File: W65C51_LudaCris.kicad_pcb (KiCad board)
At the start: 2 copper layers, 167.6 x 111.2 mm, 21 parts, among them J1 USB_RST, J2 USB_C, J3 BB816_BreakoutA27_PCIex16, J3 I2C, J5 USB_Status, J6 I2C, J7 I2C, U1 W65C51NxP, U10 74HC191, U11 ATF22V10, U12 ATF22V10, U13 74HC138, U14 74HC283, U17 MCP2221AxP, U18 MAX232, U19 74HC191, U4 74HC191, U5 74HC191, U6 1.8432 MHz, U8 74HC573, U9 74HC191

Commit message: GAL PLD
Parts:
- removed J1: USB_RST, Connector_PinHeader_2.54mm:PinHeader_1x02_P2.54mm_Horizontal
- removed J2: USB_C, Connector_USB:USB_C_Plug_JAE_DX07P024AJ1
- removed J3, J6: I2C, Connector_PinHeader_2.54mm:PinHeader_1x04_P2.54mm_Horizontal
- removed J3: BB816_BreakoutA27_PCIex16, BB816-MATX-PCIE:PCIexpress_x16_HW_FH
- removed J5: USB_Status, Connector_PinHeader_2.54mm:PinHeader_1x06_P2.54mm_Horizontal
- removed J7: I2C, Connector_PinHeader_2.54mm:PinHeader_1x03_P2.54mm_Horizontal
- removed U12: ATF22V10, Package_DIP:DIP-24_W7.62mm
- removed U13: 74HC138, Package_DIP:DIP-16_W7.62mm_Socket
- removed U14: 74HC283, Package_DIP:DIP-16_W7.62mm_Socket
- removed U17: MCP2221AxP, Package_DIP:DIP-14_W7.62mm
- removed U18: MAX232, Package_DIP:DIP-16_W7.62mm_Socket
- removed U19: 74HC191, Package_DIP:DIP-16_W7.62mm_Socket
- added C1: 100nF, Capacitor_THT:C_Disc_D3.4mm_W2.1mm_P2.50mm, F.Cu at (127.8, 132.8)
- added C10: 100nF, Capacitor_THT:C_Disc_D3.4mm_W2.1mm_P2.50mm, F.Cu at (119.3, 83.3)
- added C11: 100nF, Capacitor_THT:C_Disc_D3.4mm_W2.1mm_P2.50mm, F.Cu at (142.9, 83.3)
- added C12: 10uF, Capacitor_THT:CP_Radial_D4.0mm_P1.50mm, F.Cu at (134.8, 131.4)
- added C13: 1nF, Capacitor_THT:C_Disc_D3.4mm_W2.1mm_P2.50mm, F.Cu at (119.0, 89.9)
- added C2: 100nF, Capacitor_THT:C_Disc_D3.4mm_W2.1mm_P2.50mm, F.Cu at (137.7, 144.2)
- added C3: 100nF, Capacitor_THT:C_Disc_D3.4mm_W2.1mm_P2.50mm, F.Cu at (134.8, 128.1)
- added C4: 100nF, Capacitor_THT:C_Disc_D3.4mm_W2.1mm_P2.50mm, F.Cu at (113.4, 136.3)
- added C5: 100nF, Capacitor_THT:C_Disc_D3.4mm_W2.1mm_P2.50mm, F.Cu at (173.8, 129.0)
- added C6: 100nF, Capacitor_THT:C_Disc_D3.4mm_W2.1mm_P2.50mm, F.Cu at (94.8, 119.1)
- added C7: 100nF, Capacitor_THT:C_Disc_D3.4mm_W2.1mm_P2.50mm, F.Cu at (98.2, 96.8)
- added C8: 100nF, Capacitor_THT:C_Disc_D3.4mm_W2.1mm_P2.50mm, F.Cu at (141.5, 135.3)
- added C9: 100nF, Capacitor_THT:C_Disc_D3.4mm_W2.1mm_P2.50mm, F.Cu at (168.8, 96.6)
- added H1: MountingHole_Pad, MountingHole:MountingHole_3.2mm_M3_Pad, F.Cu at (209.2, 105.5)
- added H2: MountingHole_Pad, MountingHole:MountingHole_3.2mm_M3_Pad, F.Cu at (213.4, 145.0)
- added H3: MountingHole_Pad, MountingHole:MountingHole_3.2mm_M3_Pad, F.Cu at (212.9, 127.6)
- added R1: 50, Resistor_THT:R_Axial_DIN0207_L6.3mm_D2.5mm_P7.62mm_Horizontal, F.Cu at (118.8, 86.5)
- added U2: 74HC138, Package_DIP:DIP-16_W7.62mm_Socket, F.Cu at (134.7, 136.1)
- added U3: 74HC573, Package_DIP:DIP-20_W7.62mm_Socket, F.Cu at (142.4, 124.9)
- added U7: 74HC191, Package_DIP:DIP-16_W7.62mm_Socket, F.Cu at (87.3, 97.2)
- U10: value 74HC191 -> 74HC283
- U11: value ATF22V10 -> 74HC191; footprint Package_DIP:DIP-24_W7.62mm -> Package_DIP:DIP-16_W7.62mm_Socket
- U4, U5: value 74HC191 -> ATF22V10; footprint Package_DIP:DIP-16_W7.62mm_Socket -> Package_DIP:DIP-24_W7.62mm_Socket
- U6: value 1.8432 MHz -> 74HC191; footprint Oscillator:Oscillator_DIP-8 -> Package_DIP:DIP-16_W7.62mm_Socket
- U8: value 74HC573 -> 74HC191; footprint Package_DIP:DIP-20_W7.62mm_Socket -> Package_DIP:DIP-16_W7.62mm_Socket
- moved U5 88.2 mm to (173.7, 125.6), turned to 180 degrees
- moved U6 77.3 mm to (87.3, 123.5)
- moved U9 67.9 mm to (179.0, 100.4)
- moved U4 66.9 mm to (107.3, 132.3), turned to 180 degrees
- moved U8 55.4 mm to (144.6, 143.3), turned to 90 degrees
- moved U11 30.3 mm to (145.9, 90.9), turned to 90 degrees
- moved U10 26.7 mm to (122.2, 91.1), turned to 90 degrees
- moved U1 17.7 mm to (112.5, 96.5)
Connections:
- net /~{IRQ1} renamed /~{IRQ}
- U1 pad 10: TxD -> /TxD
- U1 pad 11: unconnected-(U1-~{DTR}-Pad11) -> /~{DTR}
- U1 pad 12: RxD -> /RxD
- U1 pad 13: /A0 -> /RS0
- U1 pad 14: /A1 -> /RS1
- U1 pad 16: GND -> /~{DCD}
- U1 pad 2: VCC -> /CS1
- U1 pad 28: /~{WR} -> /R~{W}
- U1 pad 3: /~{IOCS1} -> /~{CS2}
- U1 pad 5: unconnected-(U1-RxC-Pad5) -> /RxC
- U1 pad 7: unconnected-(U1-XTAL2-Pad7) -> /XTAL2
- U1 pad 8: unconnected-(U1-~{RTS}-Pad8) -> /~{RTS}
- U1 pad 9: GND -> /~{CTS}
- U10 pad 1: /Q9 -> Net-(U10-S2)
- U10 pad 10: /Q10 -> Net-(U10-S4)
- U10 pad 11: /~{BAUD_LOAD} -> GND
- U10 pad 12: unconnected-(U10-MAX/MIN-Pad12) -> GND
- U10 pad 13: Net-(U10-~{RCO}) -> Net-(U10-S3)
- U10 pad 14: Net-(U10-CLK) -> GND
- U10 pad 15: /Q8 -> VCC
- U10 pad 2: unconnected-(U10-Qb-Pad2) -> VCC
- U10 pad 3: unconnected-(U10-Qa-Pad3) -> /CR6
- U10 pad 4: /~{CTEN} -> Net-(U10-S1)
- U10 pad 5: VCC -> /CR5
- U10 pad 6: unconnected-(U10-Qc-Pad6) -> GND
- U10 pad 7: unconnected-(U10-Qd-Pad7) -> /CR7
- U10 pad 9: /Q11 -> unconnected-(U10-C4-Pad9)
- U11 pad 1: VCC -> Net-(U10-S2)
- U11 pad 10: GND -> Net-(U10-S3)
- U11 pad 11: GND -> /~{TX_START}
- U11 pad 12: GND -> unconnected-(U11-MAX/MIN-Pad12)
- U11 pad 13: GND -> /~{TX_COMPLETE}
- U11 pad 14: /~{CTEN} -> /~{BAUD_CLK}
- U11 pad 15: /CTL_REG_WR -> Net-(U10-S1)
- U11 pad 16: /Q8 -> VCC
- U11 pad 2: /CR0 -> unconnected-(U11-Qb-Pad2)
- U11 pad 3: /CR1 -> unconnected-(U11-Qa-Pad3)
- U11 pad 4: /CR2 -> /~{CTEN}
- U11 pad 5: /CR3 -> VCC
- U11 pad 9: GND -> Net-(U10-S4)
- U4 pad 1: Net-(U14-S2) -> VCC
- U4 pad 10: Net-(U14-S3) -> GND
- U4 pad 11: /~{TX_START} -> GND
- U4 pad 12: unconnected-(U4-MAX/MIN-Pad12) -> GND
- U4 pad 13: /~{TX_COMPLETE} -> /~{BAUD_CLK}
- U4 pad 14: /~{BAUD_CLK} -> /~{DSR}
- U4 pad 15: Net-(U14-S1) -> /~{BAUD_LOAD}
- U4 pad 16: VCC -> /~{CTEN}
- U4 pad 2: unconnected-(U4-Qb-Pad2) -> /CR0
- U4 pad 3: unconnected-(U4-Qa-Pad3) -> /CR1
- U4 pad 4: /~{CTEN} -> /CR2
- U4 pad 5: VCC -> /CR3
- U4 pad 6: unconnected-(U4-Qc-Pad6) -> /~{CTL_REG_WR}
- U4 pad 7: unconnected-(U4-Qd-Pad7) -> /~{TX_START}
- U4 pad 8: GND -> /~{TX_COMPLETE}
- U4 pad 9: Net-(U14-S4) -> GND
- U5 pad 1: /Q5 -> VCC
- U5 pad 10: /Q6 -> GND
- U5 pad 11: /~{BAUD_LOAD} -> GND
- U5 pad 12: unconnected-(U5-MAX/MIN-Pad12) -> GND
- U5 pad 13: Net-(U10-CLK) -> GND
- U5 pad 14: Net-(U19-~{RCO}) -> unconnected-(U5-I/O-Pad14)
- U5 pad 15: /Q4 -> unconnected-(U5-I/O-Pad15)
- U5 pad 16: unconnected-(U5-VCC-Pad16) -> /Q8
- U5 pad 2: unconnected-(U5-Qb-Pad2) -> /CR0
- U5 pad 3: unconnected-(U5-Qa-Pad3) -> /CR1
- U5 pad 4: /~{CTEN} -> /CR2
- U5 pad 5: VCC -> /CR3
- U5 pad 6: unconnected-(U5-Qc-Pad6) -> GND
- U5 pad 7: unconnected-(U5-Qd-Pad7) -> GND
- U5 pad 9: /Q7 -> GND
- U6 pad 1: VCC -> GND
- U6 pad 4: GND -> /~{CTEN}
- U6 pad 5: /XTAL1 -> VCC
- U6 pad 8: VCC -> GND
- U8 pad 1: GND -> /Q9
- U8 pad 10: GND -> /Q10
- U8 pad 11: /CTL_REG_WR -> /~{BAUD_LOAD}
- U8 pad 12: /CR7 -> unconnected-(U8-MAX/MIN-Pad12)
- U8 pad 13: /CR6 -> Net-(U8-~{RCO})
- U8 pad 14: /CR5 -> Net-(U7-~{RCO})
- U8 pad 15: /CR4 -> /Q8
- U8 pad 16: /CR3 -> VCC
- U8 pad 2: /D0 -> unconnected-(U8-Qb-Pad2)
- U8 pad 3: /D1 -> unconnected-(U8-Qa-Pad3)
- U8 pad 4: /D2 -> /~{CTEN}
- U8 pad 5: /D3 -> VCC
- U8 pad 6: /D4 -> unconnected-(U8-Qc-Pad6)
- U8 pad 7: /D5 -> unconnected-(U8-Qd-Pad7)
- U8 pad 8: /D6 -> GND
- U8 pad 9: /D7 -> /Q11
- U9 pad 14: Net-(U10-~{RCO}) -> Net-(U8-~{RCO})
- U9 pad 16: unconnected-(U9-VCC-Pad16) -> VCC
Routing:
- added copper zone on In1.Cu, net GND
- added copper zone on In2.Cu, net GND
- added copper zone on B.Cu, net VCC
- added copper zone on F.Cu, net VCC
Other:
- board size 167.6 x 111.2 mm -> 125.1 x 102.4 mm
- copper layers 2 -> 4

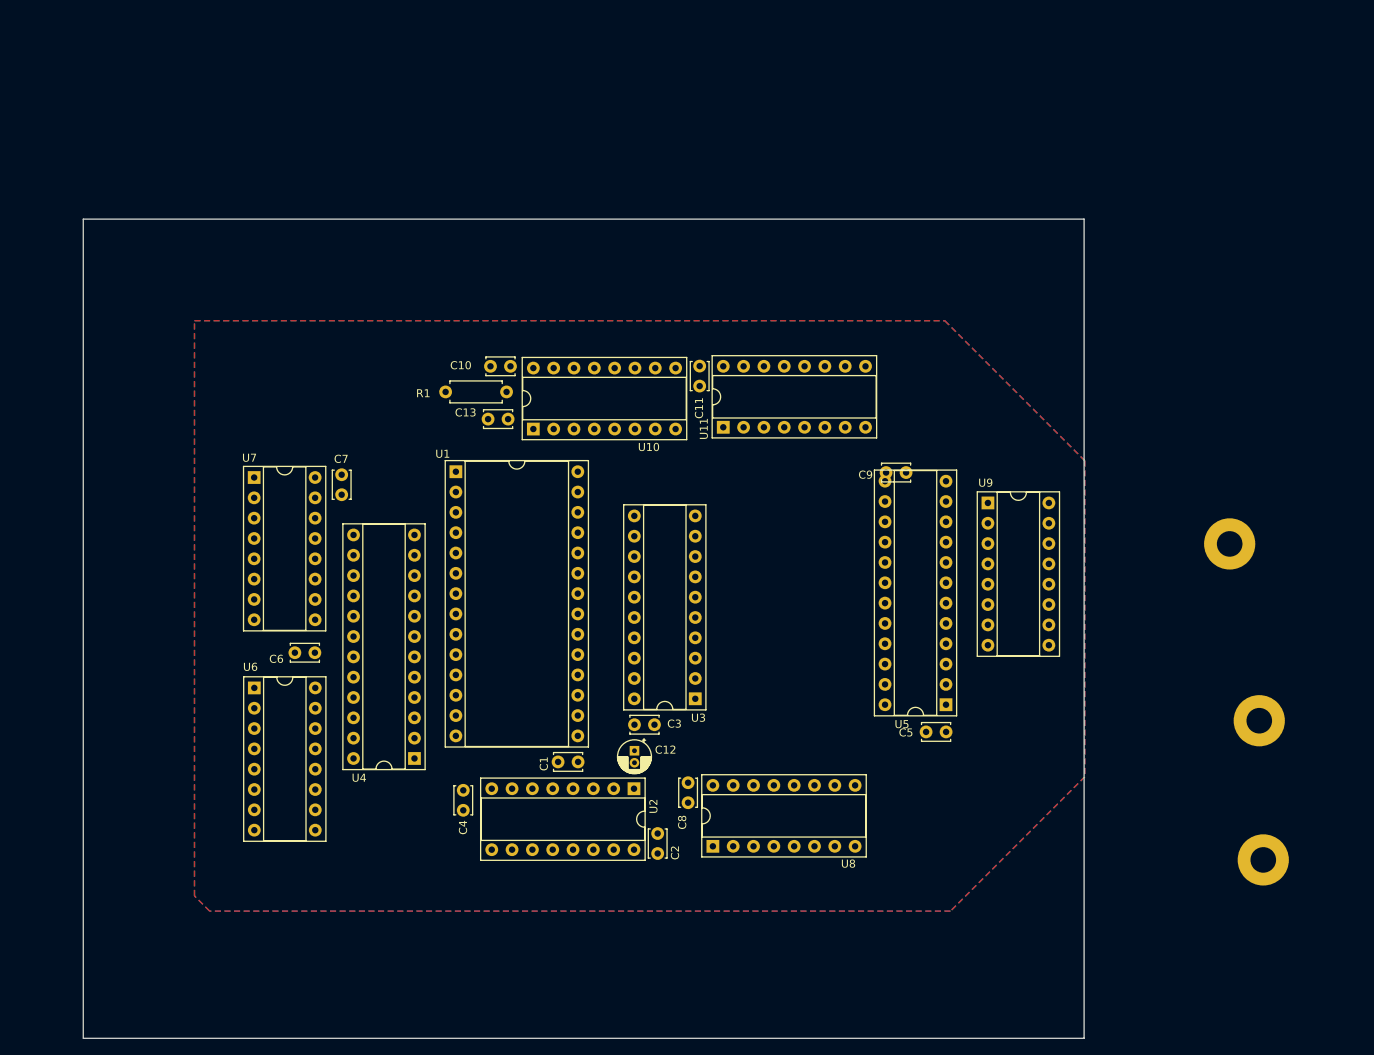
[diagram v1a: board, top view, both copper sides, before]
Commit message: PCB 2.54mm centres
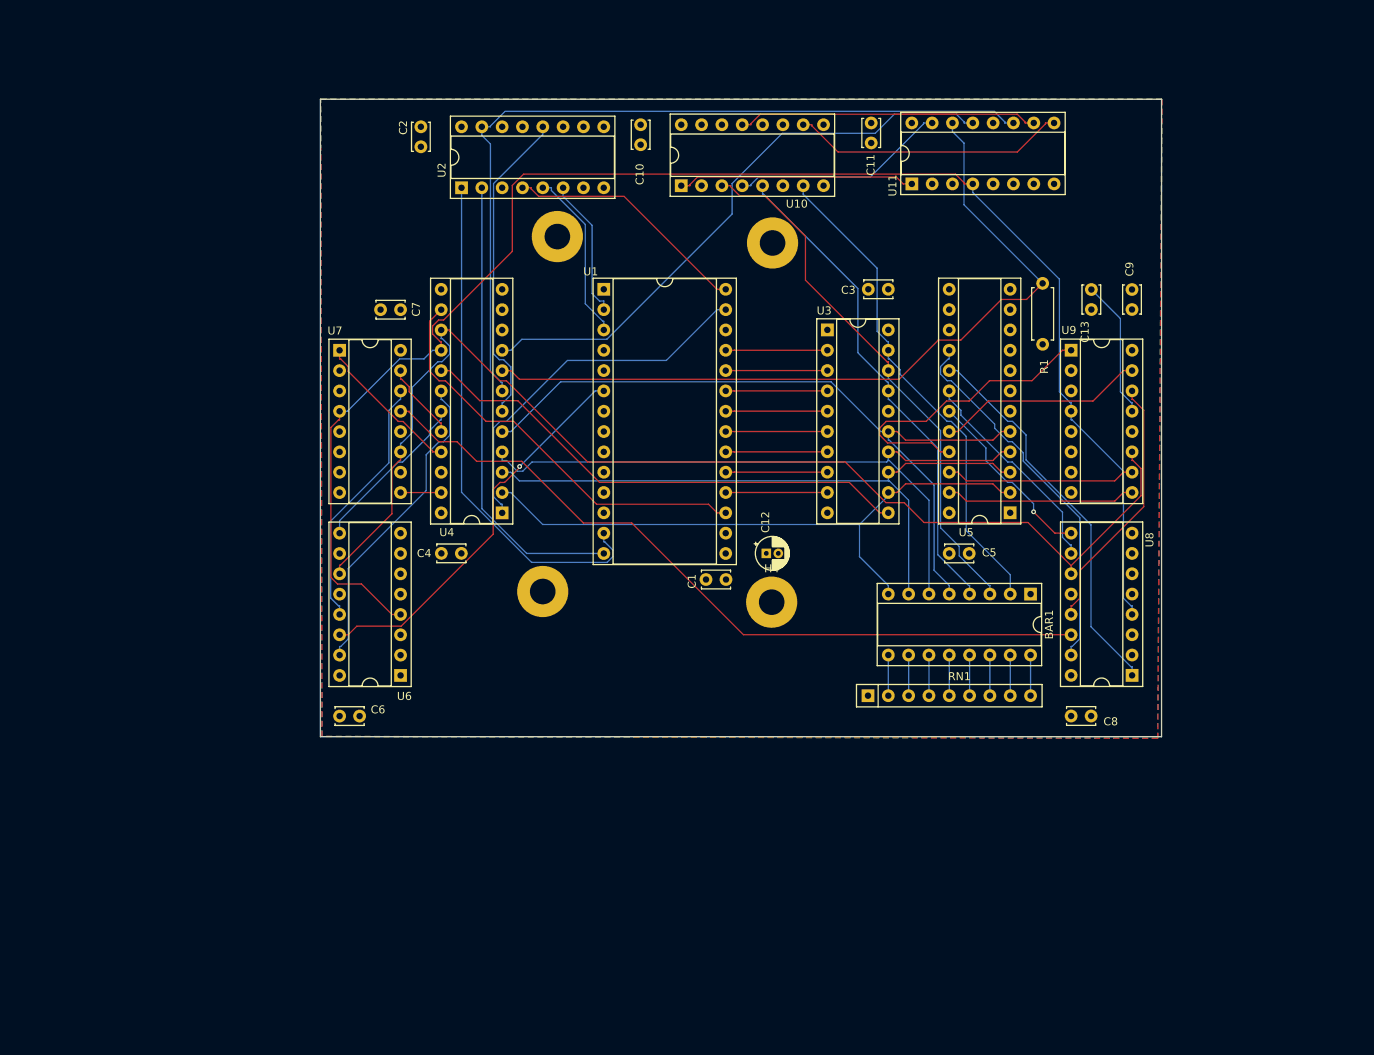
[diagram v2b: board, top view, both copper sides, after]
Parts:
- added BAR1: LED-Array-8, Package_DIP:DIP-16_W7.62mm_Socket, F.Cu at (184.3, 111.8)
- added H4: MountingHole_Pad, MountingHole:MountingHole_3.2mm_M3_Pad, F.Cu at (151.9, 112.8)
- added RN1: 220, Resistor_THT:R_Array_SIP9, F.Cu at (164.0, 124.5)
- moved H3 106.6 mm to (125.2, 67.1)
- moved H2 96.1 mm to (123.3, 111.5)
- moved C2 95.5 mm to (108.1, 53.4), turned to -90 degrees
- moved U2 78.2 mm to (113.2, 61.0), turned to 90 degrees
- moved C13 74.7 mm to (191.9, 73.7), turned to -90 degrees
- moved H1 68.4 mm to (152.1, 67.9)
- moved R1 68.4 mm to (185.8, 72.9), turned to -90 degrees
- moved C3 63.0 mm to (166.5, 73.7), turned to 180 degrees
- moved U8 56.6 mm to (197.0, 121.9), turned to 180 degrees
- moved U3 49.0 mm to (158.9, 78.8), turned to 0 degrees
- moved C8 48.6 mm to (189.4, 127.0), turned to 0 degrees
- moved U11 38.5 mm to (169.5, 60.5)
- moved C11 37.2 mm to (164.4, 52.9)
- moved U10 35.6 mm to (140.7, 60.7)
- moved C9 34.8 mm to (197.0, 76.2), turned to 90 degrees
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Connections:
- net /CTL_REG_WR renamed /CTL_REG_LOAD
- U3 pad 12: /CR7 -> /CR0
- U3 pad 13: /CR6 -> /CR1
- U3 pad 14: /CR5 -> /CR2
- U3 pad 15: /CR4 -> /CR3
- U3 pad 16: /CR3 -> /CR4
- U3 pad 17: /CR2 -> /CR5
- U3 pad 18: /CR1 -> /CR6
- U3 pad 19: /CR0 -> /CR7
- U3 pad 2: /D0 -> /D7
- U3 pad 3: /D1 -> /D6
- U3 pad 4: /D2 -> /D5
- U3 pad 5: /D3 -> /D4
- U3 pad 6: /D4 -> /D3
- U3 pad 7: /D5 -> /D2
- U3 pad 8: /D6 -> /D1
- U3 pad 9: /D7 -> /D0
- U4 pad 1: VCC -> /CLK
- U4 pad 13: /~{BAUD_CLK} -> GND
- U4 pad 8: /~{TX_COMPLETE} -> /~{BAUD_CLK}
- U4 pad 9: GND -> /~{TX_COMPLETE}
- U5 pad 1: VCC -> GND
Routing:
- net /~{CTEN}: track 0.00 -> 194.5 mm
- net /~{BAUD_LOAD}: track 0.00 -> 147.6 mm
- net /~{BAUD_CLK}: track 0.00 -> 121.5 mm
- net /~{TX_START}: track 0.00 -> 102.1 mm
- net Net-(U7-~{RCO}): track 0.00 -> 95.5 mm
- net /CR3: track 0.00 -> 93.2 mm
- net /CR2: track 0.00 -> 86.5 mm
- net /CR1: track 0.00 -> 81.2 mm
- net /CR0: track 0.00 -> 78.1 mm
- net /~{TX_COMPLETE}: track 0.00 -> 73.8 mm
- net /CR6: track 0.00 -> 67.6 mm
- net /RS0: track 0.00 -> 64.4 mm
- net /CTL_REG_LOAD: track 0.00 -> 63.3 mm
- net /CR7: track 0.00 -> 62.2 mm
- net /CR5: track 0.00 -> 62.1 mm
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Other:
- board size 125.1 x 102.4 mm -> 105.1 x 79.7 mm

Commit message: pcb
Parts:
- removed BAR1: LED-Array-8, Package_DIP:DIP-16_W7.62mm_Socket
- removed RN1: 220, Resistor_THT:R_Array_SIP9
- added J1: Conn_01x14, Connector_PinHeader_2.54mm:PinHeader_1x14_P2.54mm_Vertical, B.Cu at (133.5, 73.7)
- added J2: Conn_01x14, Connector_PinHeader_2.54mm:PinHeader_1x14_P2.54mm_Vertical, B.Cu at (148.8, 73.7)
- moved C2 60.8 mm to (119.1, 113.1), turned to 90 degrees
- moved U2 57.8 mm to (122.1, 118.1)
- moved U8 41.4 mm to (155.9, 117.2), turned to 90 degrees
- moved C8 39.6 mm to (155.9, 105.8)
- moved C10 38.3 mm to (170.0, 69.8), turned to 90 degrees
- moved U11 34.6 mm to (134.9, 62.3), turned to -90 degrees
- moved C11 30.8 mm to (138.7, 69.9), turned to 90 degrees
- moved H4 27.6 mm to (179.5, 113.5)
- moved H1 26.1 mm to (178.1, 65.8)
- moved U10 26.0 mm to (166.6, 62.2), turned to -90 degrees
- moved H2 22.8 mm to (145.8, 115.6)
- moved C13 17.6 mm to (176.3, 81.9), turned to 180 degrees
- moved C9 16.3 mm to (181.7, 81.9), turned to 180 degrees
- moved U9 16.1 mm to (174.1, 86.4)
- moved H3 15.9 mm to (109.6, 63.7)
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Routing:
- net /~{TX_COMPLETE}: track 73.8 -> 12.3 mm
- net /~{TX_START}: track 102.1 -> 44.1 mm
- net /CR3: track 93.2 -> 45.0 mm
- net /~{CTEN}: track 194.5 -> 148.3 mm
- net /CR6: track 67.6 -> 22.7 mm
- net /RS0: track 64.4 -> 20.2 mm
- net /CR2: track 86.5 -> 45.0 mm
- net /RS1: track 57.7 -> 16.7 mm
- net /CR7: track 62.2 -> 22.2 mm
- net /~{BAUD_CLK}: track 121.5 -> 83.2 mm
- net /CR1: track 81.2 -> 45.0 mm
- net /CR0: track 78.1 -> 45.0 mm
- net /~{BAUD_LOAD}: track 147.6 -> 115.6 mm
- net /CR5: track 62.1 -> 33.2 mm
- net /R~{W}: track 30.7 -> 59.3 mm
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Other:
- board size 105.1 x 79.7 mm -> 78.9 x 62.6 mm
